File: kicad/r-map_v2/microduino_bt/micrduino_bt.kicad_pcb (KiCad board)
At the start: 2 copper layers, 25.4 x 27.9 mm, 13 parts, among them P1 CONN_01X01, P2 CONN_01X01, P3 CONN_01X01, P4 CONN_01X01, P5 CONN_01X01, P6 CONN_01X01, U1 Microduino, U2 ITEAD_HC-05

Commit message: Add files from last commit on sourceforge
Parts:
- removed P1, P2, P4, P5, P6: CONN_01X01, Measurement_Points:Measurement_Point_Square-SMD-Pad_Small
- removed R4: 10K, w_smd_resistors:r_0805
- D1: value LED -> LED-
- turned D1 to 90 degrees
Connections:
- net Net-(P3-Pad1) renamed /SET
- D1 pad 2: Net-(D1-Pad2) -> /LED
- R3 pad 1: Net-(D1-Pad2) -> Net-(D1-Pad1)
- U1 pad 6: (no net) -> Net-(R1-Pad1)
- U1 pad 7: (no net) -> Net-(U1-Pad7)
- U1 pad 8: Net-(R1-Pad1) -> (no net)
- U1 pad 9: Net-(U1-Pad9) -> (no net)
- U2 pad 1: Net-(U1-Pad9) -> Net-(U1-Pad7)
- U2 pad 24: Net-(P4-Pad1) -> /LED
- U2 pad 26: Net-(P1-Pad1) -> (no net)
- U2 pad 31: Net-(P6-Pad1) -> /LED
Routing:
- net Net-(U1-Pad9): track 36.0 -> 0.00 mm, vias 1 -> 0
- net Net-(U1-Pad7): track 0.00 -> 35.9 mm
- net GND: track 76.1 -> 51.9 mm
- net Net-(P2-Pad1): track 23.6 -> 0.00 mm
- net /LED: track 0.00 -> 22.3 mm, vias 0 -> 1
- net Net-(P1-Pad1): track 9.72 -> 0.00 mm, vias 1 -> 0
- net Net-(P6-Pad1): track 9.32 -> 0.00 mm, vias 1 -> 0
- net Net-(D1-Pad2): track 8.38 -> 0.00 mm
- net Net-(P4-Pad1): track 4.61 -> 0.00 mm, vias 1 -> 0
- net Net-(R1-Pad2): track 18.3 -> 20.5 mm
- net /SET: track 7.66 -> 5.85 mm
- net Net-(D1-Pad1): track 9.88 -> 8.58 mm
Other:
- board text added: "SET"

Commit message: Sistemato orientamento case led smd, generati files gbr per i2c hub e breakout board
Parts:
- D1: value LED- -> LED
- turned D1 to 270 degrees
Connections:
- net Net-(R1-Pad1) renamed /INT_28J60
- net Net-(U1-Pad7) renamed /RX1
- D1 pad 1: Net-(D1-Pad1) -> /LED
- D1 pad 2: /LED -> Net-(D1-Pad2)
- R3 pad 1: Net-(D1-Pad1) -> Net-(D1-Pad2)
- U1 pad 10: (no net) -> Net-(U1-Pad10)
- U1 pad 11: (no net) -> Net-(U1-Pad11)
- U1 pad 12: (no net) -> /SCL
- U1 pad 13: (no net) -> /SDA
- U1 pad 14: (no net) -> Net-(U1-Pad14)
- U1 pad 15: (no net) -> Net-(U1-Pad15)
- U1 pad 16: (no net) -> Net-(U1-Pad16)
- U1 pad 17: (no net) -> Net-(U1-Pad17)
- U1 pad 18: (no net) -> Net-(U1-Pad18)
- U1 pad 19: (no net) -> /SCK
- U1 pad 2: (no net) -> Net-(U1-Pad2)
- U1 pad 20: (no net) -> /MISO
- U1 pad 21: (no net) -> /MOSI
- U1 pad 22: (no net) -> /CS_NRF24
- U1 pad 23: (no net) -> /CE_NRF24
- U1 pad 24: (no net) -> /CONFIG
- U1 pad 25: (no net) -> Net-(U1-Pad25)
- U1 pad 27: (no net) -> Net-(U1-Pad27)
- U1 pad 3: (no net) -> Net-(U1-Pad3)
- U1 pad 4: (no net) -> Net-(U1-Pad4)
- U1 pad 5: (no net) -> Net-(U1-Pad5)
- U1 pad 8: (no net) -> Net-(U1-Pad8)
- U1 pad 9: (no net) -> Net-(U1-Pad9)
- U2 pad 10: (no net) -> Net-(U2-Pad10)
- U2 pad 11: (no net) -> Net-(U2-Pad11)
- U2 pad 15: (no net) -> Net-(U2-Pad15)
- U2 pad 16: (no net) -> Net-(U2-Pad16)
- U2 pad 17: (no net) -> Net-(U2-Pad17)
- U2 pad 18: (no net) -> Net-(U2-Pad18)
- U2 pad 19: (no net) -> Net-(U2-Pad19)
- U2 pad 20: (no net) -> Net-(U2-Pad20)
- U2 pad 23: (no net) -> Net-(U2-Pad23)
- U2 pad 25: (no net) -> Net-(U2-Pad25)
- U2 pad 26: (no net) -> Net-(U2-Pad26)
- U2 pad 27: (no net) -> Net-(U2-Pad27)
- U2 pad 28: (no net) -> Net-(U2-Pad28)
- U2 pad 29: (no net) -> Net-(U2-Pad29)
- U2 pad 3: (no net) -> Net-(U2-Pad3)
- U2 pad 30: (no net) -> Net-(U2-Pad30)
- U2 pad 32: (no net) -> Net-(U2-Pad32)
- U2 pad 33: (no net) -> Net-(U2-Pad33)
- U2 pad 4: (no net) -> Net-(U2-Pad4)
- U2 pad 5: (no net) -> Net-(U2-Pad5)
- U2 pad 6: (no net) -> Net-(U2-Pad6)
- U2 pad 7: (no net) -> Net-(U2-Pad7)
- U2 pad 8: (no net) -> Net-(U2-Pad8)
- U2 pad 9: (no net) -> Net-(U2-Pad9)
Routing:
- net Net-(D1-Pad2): track 0.00 -> 8.58 mm
- net Net-(D1-Pad1): track 8.58 -> 0.00 mm

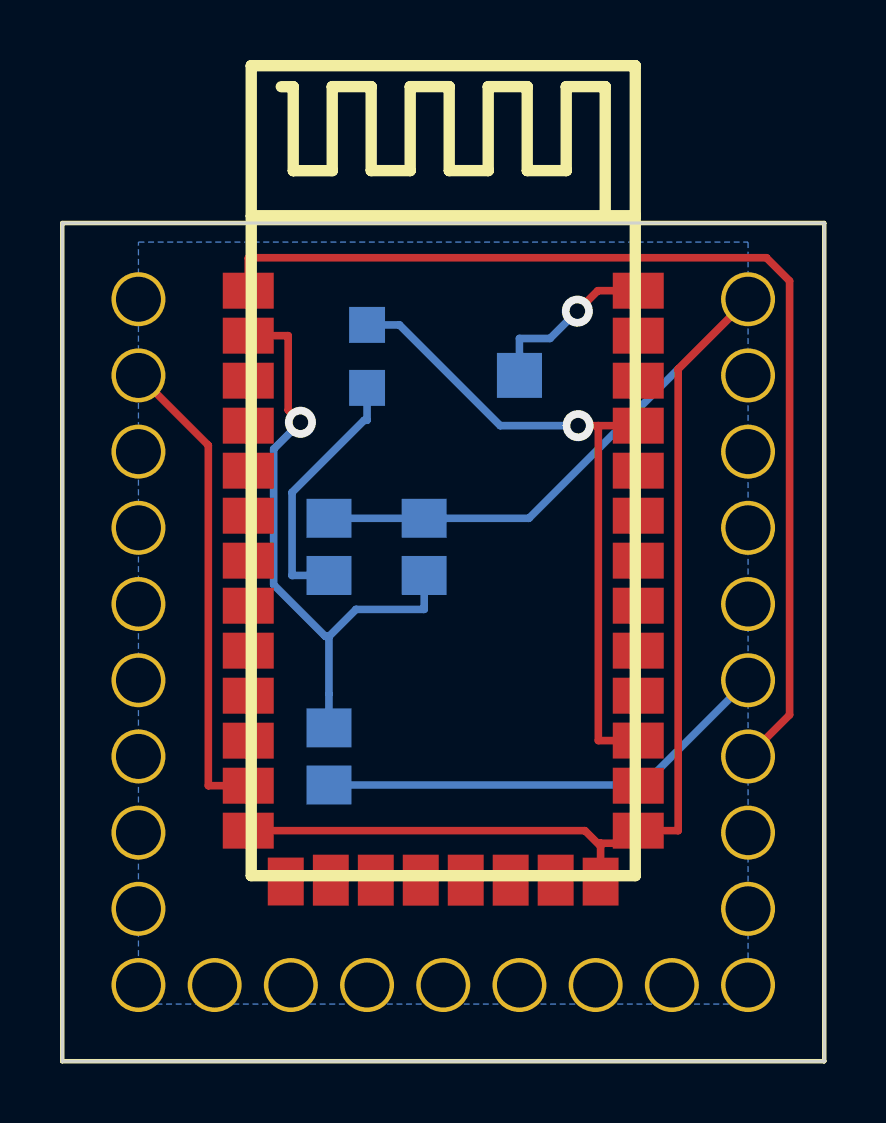
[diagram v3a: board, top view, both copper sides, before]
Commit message: Nouva versione pcb, doppia schermatura, allargamento piste, rimozione connessioni T ed Y
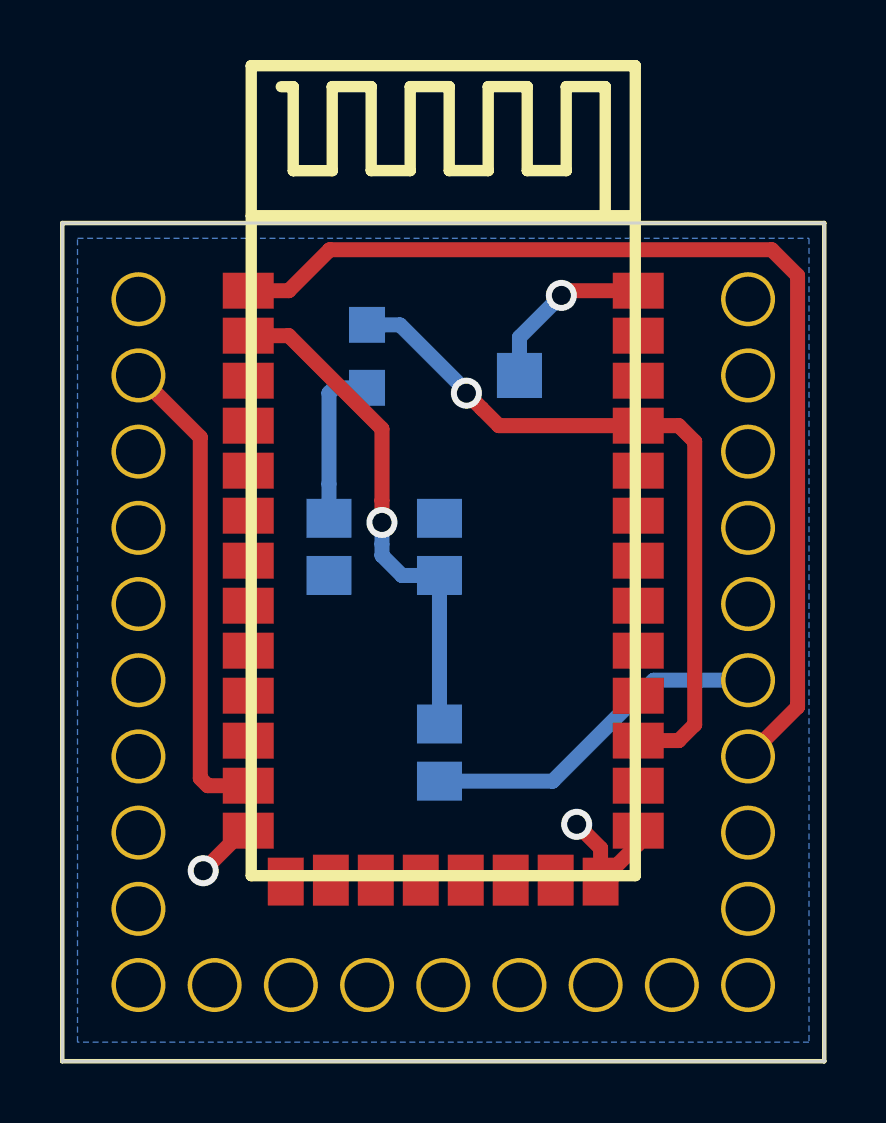
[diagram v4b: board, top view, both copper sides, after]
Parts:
- moved R1 3.69 mm to (148.5, 107.2)
- moved R2 0.51 mm to (148.5, 100.3)
- turned R3 to 90 degrees
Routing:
- net GND: track 51.9 -> 7.60 mm, vias 0 -> 2
- net /INT_28J60: track 15.4 -> 11.7 mm
- net Net-(R1-Pad2): track 20.5 -> 17.1 mm
- net Net-(D1-Pad2): track 8.58 -> 5.52 mm
- net /LED: track 22.3 -> 24.3 mm
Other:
- net class Futura added: clearance 0.5, trace_width 0.5, via_dia 1.035, via_drill 0.635
